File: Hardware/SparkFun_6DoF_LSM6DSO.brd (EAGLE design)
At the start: 25.4 x 25.4 mm, 61 parts, among them J1 QWIIC_RIGHT_ANGLE, J2 QWIIC_RIGHT_ANGLE, U2 LSM6DS0

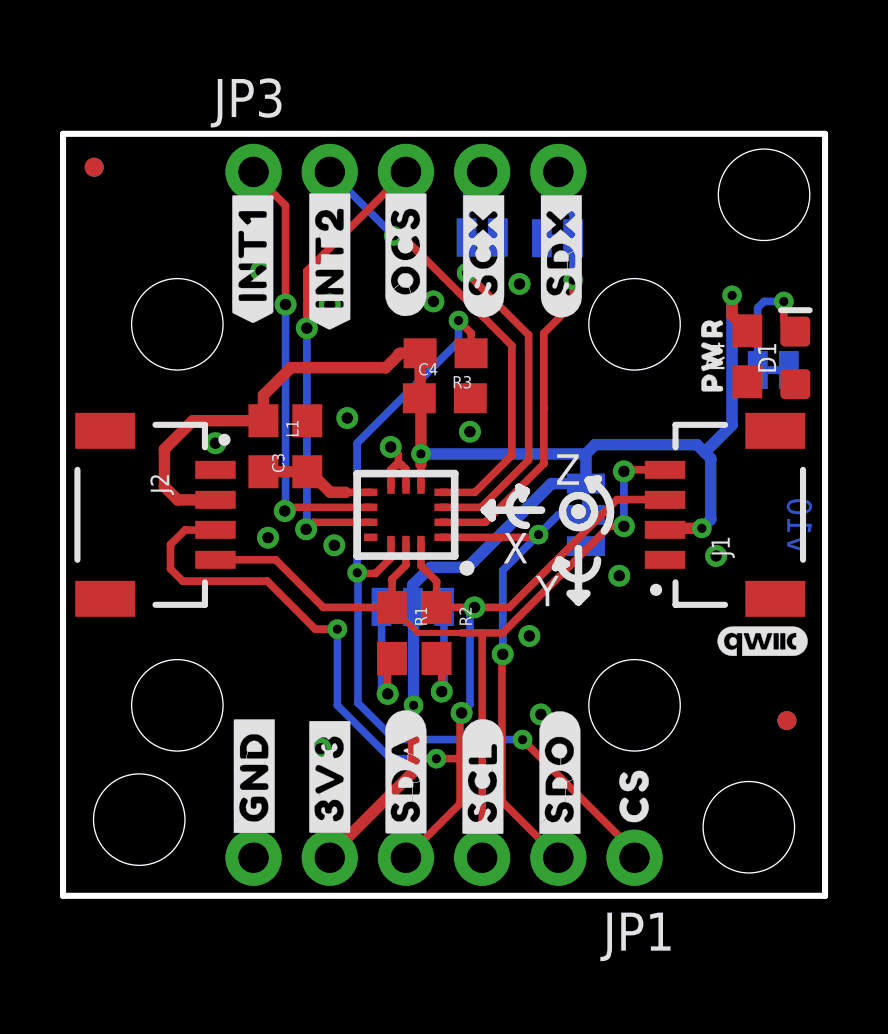
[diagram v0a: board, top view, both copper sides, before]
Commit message: Fixes input/output labels of respective silk, adds better text description to jumpers
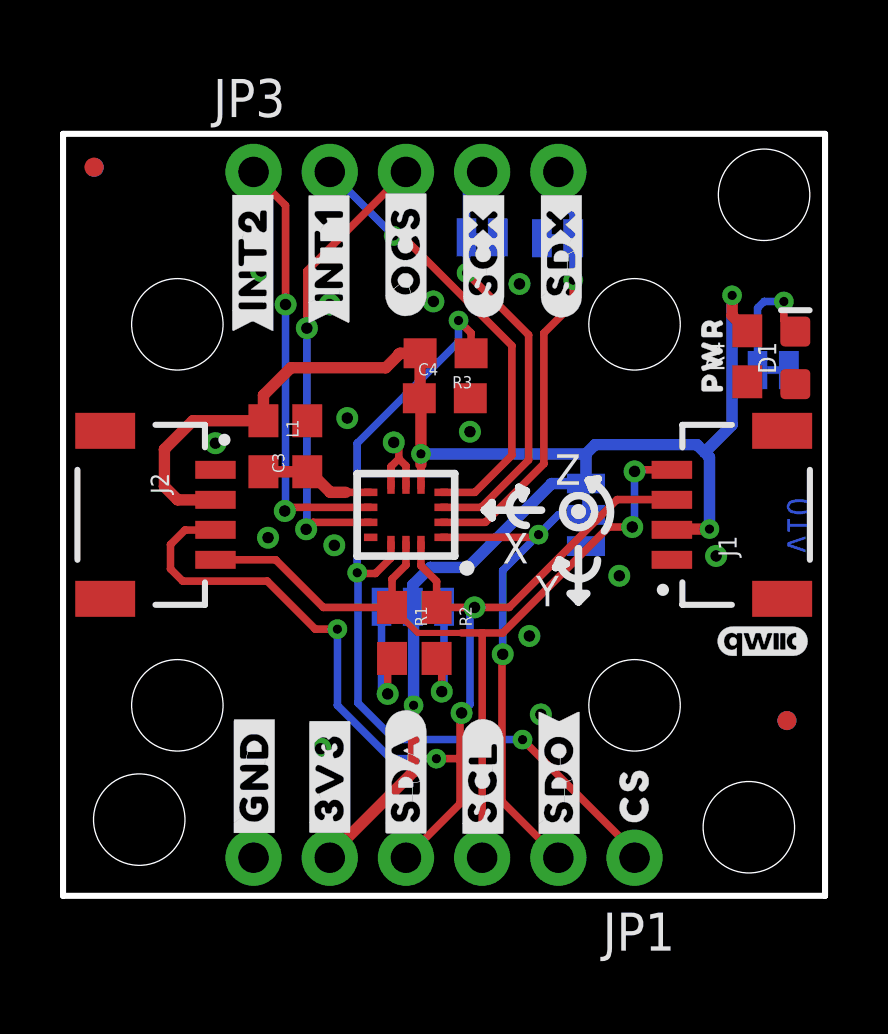
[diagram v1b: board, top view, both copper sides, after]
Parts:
- U$18: device bot:#INT1#7 -> bot:#SDO#7
- U$19: device bot:#INT2#7 -> bot:#INT1#9
- U$21: device bot:#SA0#7 -> bot:#INT2#9
- U$7: device top:#INT1#8 -> top:#INT1#9
- U$8: device top:#INT2#8 -> top:#INT2#9
- moved U$18 20.2 mm to (16.5, 3.94)
- moved U$21 20.1 mm to (6.32, 21.3)
- moved U$8 2.57 mm to (6.32, 21.3)
- moved U$7 2.54 mm to (8.86, 21.4)
- moved U$14 1.24 mm to (14.8, 13.3)
- moved U$13 1.14 mm to (14.7, 12.1)
- moved J1 0.23 mm to (20.3, 12.7)
- moved U$19 0.08 mm to (8.86, 21.4)
- renumbered JP2 to LED, U2 to U1

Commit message: Adds VDD and VDDIO voltage range to schematic
* Moves some traces and vias that were too close to the standoffs
* Adds SparkFun flame and name of product to topside
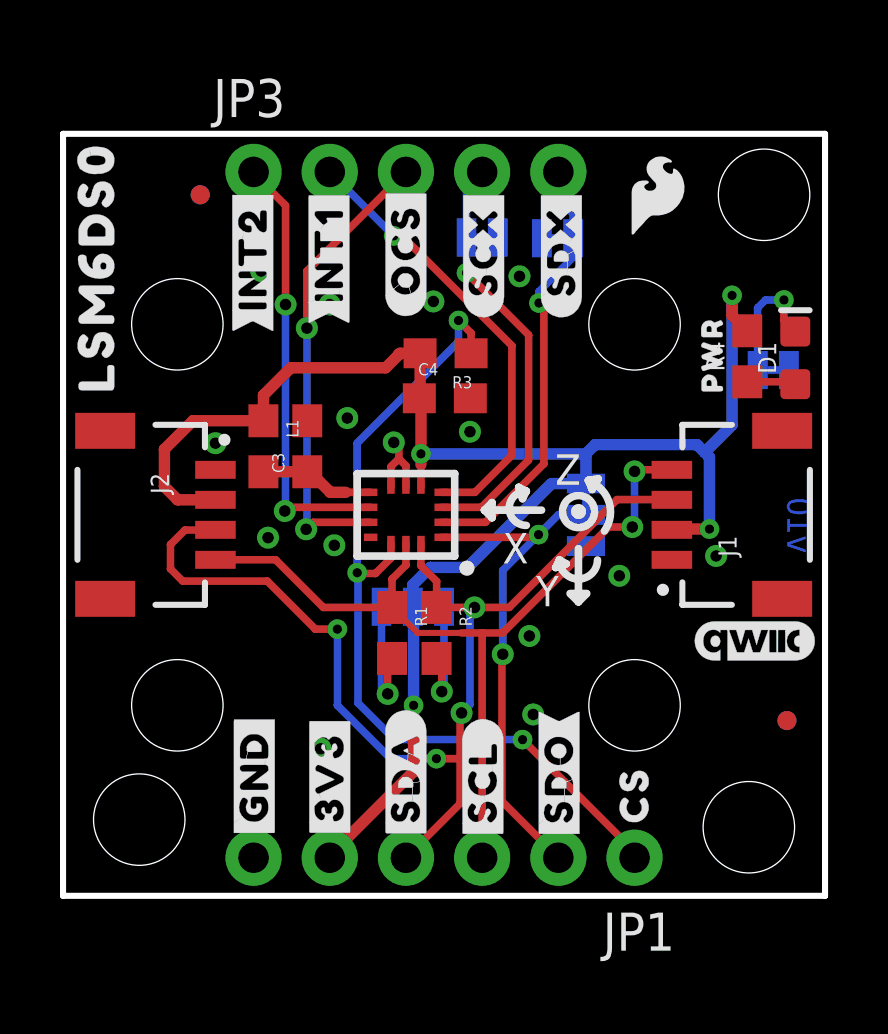
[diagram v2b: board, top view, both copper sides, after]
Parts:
- added U$29: (no value), SparkFun-Aesthetics:SFE_LOGO_FLAME_.1
- added U$30: (no value), top:LSM6DS011
- LOGO1: value QWIIC_LOGO_3MM -> QWIIC_LOGO_4MM; device SparkFun-Aesthetics:QWIIC_3MM -> SparkFun-Aesthetics:QWIIC_4MM
- moved FRAME1 17.8 mm to (-19.1, -11.4)
- moved FID1 3.66 mm to (4.57, 23.4)
- moved FD1 3.65 mm to (4.57, 23.4)
- moved LOGO1 0.25 mm to (23.1, 8.48)
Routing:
- net N$2: track 0.00 -> 1.63 mm
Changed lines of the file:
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@@
 <setting verticaltext="up"/>
 </settings>
-<grid distance="0.01" unitdist="inch" unit="inch" style="dots" multiple="1" display="yes" altdistance="0.001" altunitdist="inch" altunit="inch"/>
+<grid distance="0.05" unitdist="inch" unit="inch" style="dots" multiple="1" display="yes" altdistance="0.005" altunitdist="inch" altunit="inch"/>
 <layers>
 <layer number="1" name="Top" color="4" fill="1" visible="yes" active="yes"/>
@@
 <wire x1="5.3959125" y1="13.3937375" x2="6.1102875" y2="12.6793625" width="0.2032" layer="22"/>
 <wire x1="6.0706" y1="13.3937375" x2="5.356225" y2="12.6793625" width="0.2032" layer="22"/>
-<text x="-7.62" y="-31.75" size="1.778" layer="51" font="vector">Revised By: Elias Santistevan</text>
+<text x="-7.62" y="-13.97" size="1.778" layer="51" font="vector">Revised By: Elias Santistevan</text>
 <rectangle x1="15.7734" y1="22.86" x2="17.1958" y2="23.3934" layer="22"/>
 <rectangle x1="13.2334" y1="22.9108" x2="14.6304" y2="23.4188" layer="22"/>
@@
 </autorouter>
 <elements>
-<element name="FRAME1" library="SparkFun-Aesthetics" package="CREATIVE_COMMONS" value="FRAME-LETTER" x="-19.05" y="-29.21" smashed="yes">
-<attribute name="DESIGNER" value="Marshall Taylor" x="12.7" y="-29.21" size="1.778" layer="51" font="vector"/>
-<attribute name="REV" value="" x="-19.05" y="-29.21" size="1.778" layer="27" display="off"/>
+<element name="FRAME1" library="SparkFun-Aesthetics" package="CREATIVE_COMMONS" value="FRAME-LETTER" x="-19.05" y="-11.43" smashed="yes">
+<attribute name="DESIGNER" value="Marshall Taylor" x="12.7" y="-11.43" size="1.778" layer="51" font="vector"/>
+<attribute name="REV" value="" x="-19.05" y="-11.43" size="1.778" layer="27" display="off"/>
 </element>
 <element name="C3" library="SparkFun-Capacitors" package="0603" value="0.1uF" x="8.1407" y="14.986" smashed="yes" rot="R90">
@@
 <attribute name="VALUE" value="30Ω" x="5.5372" y="16.002" size="0.4064" layer="27" font="vector" rot="R270"/>
 </element>
-<element name="FID1" library="SparkFun-Aesthetics" package="FIDUCIAL-MICRO" value="FIDUCIALUFIDUCIAL" x="1.031875" y="24.28875" smashed="yes"/>
+<element name="FID1" library="SparkFun-Aesthetics" package="FIDUCIAL-MICRO" value="FIDUCIALUFIDUCIAL" x="4.572" y="23.368" smashed="yes"/>
 <element name="FID2" library="SparkFun-Aesthetics" package="FIDUCIAL-MICRO" value="FIDUCIALUFIDUCIAL" x="24.13" y="5.842" smashed="yes"/>
 <element name="R3" library="SparkFun-Resistors" package="0603" value="10k" x="12.7508" y="18.0848" smashed="yes" rot="R180">
@@
 <attribute name="VALUE" x="23.5966" y="11.049" size="0.6096" layer="27" font="vector" ratio="20" rot="R90"/>
 </element>
-<element name="FD1" library="SparkFun-Aesthetics" package="FIDUCIAL-MICRO" value="FIDUCIALUFIDUCIAL" x="1.0414" y="24.2824" smashed="yes" rot="MR0"/>
+<element name="FD1" library="SparkFun-Aesthetics" package="FIDUCIAL-MICRO" value="FIDUCIALUFIDUCIAL" x="4.572" y="23.368" smashed="yes" rot="MR0"/>
 <element name="FD2" library="SparkFun-Aesthetics" package="FIDUCIAL-MICRO" value="FIDUCIALUFIDUCIAL" x="24.13" y="5.842" smashed="yes" rot="MR0"/>
-<element name="LOGO1" library="SparkFun-Aesthetics" package="QWIIC_3MM" value="QWIIC_LOGO_3MM" x="23.3172" y="8.4836" smashed="yes"/>
+<element name="LOGO1" library="SparkFun-Aesthetics" package="QWIIC_4MM" value="QWIIC_LOGO_4MM" x="23.0632" y="8.4836" smashed="yes"/>
 <element name="U$1" library="top" package="#3V3#1" value="" x="8.89" y="3.9624" smashed="yes" rot="R90"/>
 <element name="U$2" library="top" package="#GND#0" value="" x="6.3754" y="3.9878" smashed="yes" rot="R90"/>
@@
 <element name="U$21" library="bot" package="#INT2#9" value="" x="6.3246" y="21.2598" smashed="yes" rot="MR270"/>
 <element name="U$26" library="bot" package="#SDI#4" value="" x="11.43" y="3.6068" smashed="yes" rot="MR270"/>
+<element name="U$29" library="SparkFun-Aesthetics" package="SFE_LOGO_FLAME_.1" value="" x="19.812" y="23.368" smashed="yes"/>
+<element name="U$30" library="top" package="LSM6DS011" value="" x="1.1176" y="20.9804" smashed="yes" rot="R90"/>
 </elements>
 <signals>
@@
 <contactref element="J1" pad="1"/>
 <via x="9.4742" y="15.9258" extent="1-16" drill="0.381"/>
-<via x="15.2146" y="20.3962" extent="1-16" drill="0.381"/>
+<via x="15.2146" y="20.6502" extent="1-16" drill="0.381"/>
 <via x="18.542" y="10.668" extent="1-16" drill="0.381"/>
 <via x="8.5852" y="4.9022" extent="1-16" drill="0.381"/>
@@
 <via x="5.08" y="15.0876" extent="1-16" drill="0.381"/>
 <via x="13.5636" y="15.4686" extent="1-16" drill="0.381"/>
-<via x="15.9258" y="6.0452" extent="1-16" drill="0.381"/>
+<via x="15.6718" y="6.0452" extent="1-16" drill="0.381"/>
 <via x="15.5448" y="8.6614" extent="1-16" drill="0.381"/>
 <via x="12.3444" y="19.812" extent="1-16" drill="0.381"/>
@@
 <contactref element="SDX" pad="2"/>
 <wire x1="14.0756" y1="12.45" x2="16.0274" y2="14.4018" width="0.254" layer="1"/>
-<wire x1="17.0053" y1="20.5232" x2="17.0053" y2="21.9202" width="0.254" layer="16"/>
-<wire x1="17.0053" y1="20.5232" x2="17.0053" y2="19.7358" width="0.254" layer="1"/>
-<wire x1="17.0053" y1="19.7358" x2="16.0274" y2="18.7579" width="0.254" layer="1"/>
-<wire x1="16.0274" y1="18.7579" x2="16.0274" y2="14.4018" width="0.254" layer="1"/>
+<wire x1="17.0053" y1="21.2852" x2="17.0053" y2="21.9202" width="0.254" layer="16"/>
+<wire x1="17.0053" y1="21.2852" x2="15.8623" y2="20.1422" width="0.254" layer="16"/>
+<wire x1="15.8623" y1="20.1422" x2="15.8623" y2="19.7612" width="0.254" layer="16"/>
+<wire x1="15.8623" y1="19.7612" x2="16.0274" y2="19.5961" width="0.254" layer="1"/>
+<wire x1="16.0274" y1="19.5961" x2="16.0274" y2="14.4018" width="0.254" layer="1"/>
 <wire x1="17.0053" y1="21.9202" x2="17.0053" y2="22.733" width="0.254" layer="16"/>
 <wire x1="17.0053" y1="22.733" x2="16.51" y2="23.2283" width="0.254" layer="16"/>
 <wire x1="16.51" y1="23.2283" x2="16.51" y2="24.13" width="0.254" layer="16"/>
-<via x="17.0053" y="20.5232" extent="1-16" drill="0.3048"/>
+<via x="15.8623" y="19.7612" extent="1-16" drill="0.3048"/>
 <contactref element="U1" pad="2"/>
 <wire x1="12.605" y1="12.45" x2="14.0756" y2="12.45" width="0.254" layer="1"/>
@@
 <wire x1="17.43075" y1="14.732" x2="17.73555" y2="15.0368" width="0.381" layer="16"/>
 <wire x1="17.73555" y1="15.0368" x2="21.1328" y2="15.0368" width="0.381" layer="16"/>
-<wire x1="11.93" y1="14.3764" x2="11.938" y2="14.3764" width="0.254" layer="1"/>
 <wire x1="11.93" y1="14.732" x2="11.93" y2="14.3764" width="0.381" layer="1"/>
 <contactref element="R4" pad="2"/>
@@
 <contactref element="R4" pad="1"/>
 <contactref element="D1" pad="A"/>
-<wire x1="22.8092" y1="17.1332" x2="24.4094" y2="17.0554" width="0" layer="19" extent="1-1"/>
+<wire x1="22.8092" y1="17.1332" x2="24.3316" y2="17.1332" width="0.254" layer="1"/>
+<wire x1="24.3316" y1="17.1332" x2="24.4094" y2="17.0554" width="0.254" layer="1"/>
 </signal>
 <signal name="N$3">
@@
 <contactref element="LED" pad="2"/>
 <wire x1="24.4094" y1="18.8094" x2="24.0284" y2="19.1904" width="0.254" layer="1"/>
-<wire x1="24.0284" y1="19.1904" x2="24.0284" y2="19.812" width="0.254" layer="1"/>
-<via x="24.0284" y="19.812" extent="1-16" drill="0.3048"/>
-<wire x1="24.0284" y1="19.812" x2="23.368" y2="19.812" width="0.254" layer="16"/>
-<wire x1="23.368" y1="19.812" x2="23.1521" y2="19.5961" width="0.254" layer="16"/>
+<wire x1="24.0284" y1="19.1904" x2="24.0284" y2="19.8628" width="0.254" layer="1"/>
+<via x="24.0284" y="19.8628" extent="1-16" drill="0.3048"/>
+<wire x1="24.0284" y1="19.8628" x2="23.4188" y2="19.8628" width="0.254" layer="16"/>
+<wire x1="23.4188" y1="19.8628" x2="23.1521" y2="19.5961" width="0.254" layer="16"/>
 <wire x1="23.1521" y1="19.5961" x2="23.1521" y2="17.526" width="0.254" layer="16"/>
 </signal>

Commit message: Updates LSM6D0 with axes, fixes measures, removes references to "slave/master" terminology
* Removes inner standoffs
* Centers IC
* Adds 100k pullup to SDO/SA0 net
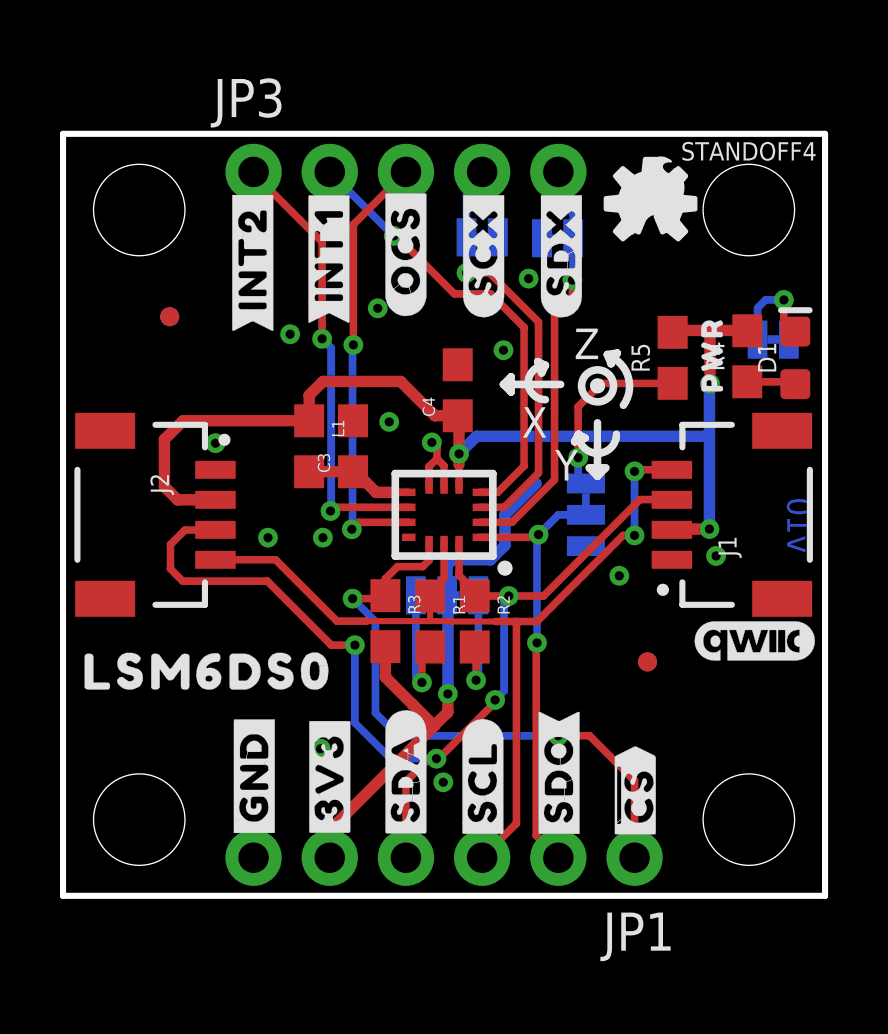
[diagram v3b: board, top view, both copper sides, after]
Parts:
- removed STANDOFF5, STANDOFF6, STANDOFF7: STAND-OFFTIGHT, SparkFun-Hardware:STAND-OFF-TIGHT
- added R5: 100k, SparkFun-Resistors:0603
- added U$31: (no value), top:6DOF12
- U$27: device top:CS7 -> bot:##CS##8
- U$3: device bot:CS7 -> top:##CS##7
- moved LOGO2 17.0 mm to (19.6, 23.1), flipped to the top
- moved STANDOFF3 16.9 mm to (22.9, 2.54)
- moved STANDOFF4 16.9 mm to (22.9, 22.9)
- moved U$30 14.0 mm to (4.85, 7.47), turned to 0 degrees
- moved R3 9.15 mm to (10.7, 9.16), turned to 270 degrees
- moved U$12 6.26 mm to (7.59, 11.9)
- moved LOGO3 6.22 mm to (4.12, 12.8), turned to 270 degrees
- moved FD2 5.04 mm to (19.5, 7.80)
- moved FID2 5.04 mm to (19.5, 7.80)
- moved FD1 4.19 mm to (3.56, 19.3)
- moved FID1 4.19 mm to (3.56, 19.3)
- moved STANDOFF2 4.02 mm to (2.54, 2.54)
- moved STANDOFF1 4.02 mm to (2.54, 22.9)
- moved L1 1.52 mm to (8.20, 15.0)
- moved C3 1.52 mm to (9.66, 15.0)
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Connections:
- net CS renamed !CS!
- new net N$1: ADDR.3, R5.1
- net 3.3V: now also R5.2; no longer ADDR.3
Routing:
- net !CS!: track 28.8 -> 20.3 mm, vias 3 -> 2
- net N$1: track 0.00 -> 6.14 mm, vias 0 -> 1
- net SDO/SA0: track 17.2 -> 15.0 mm
- net SCL: track 29.4 -> 31.0 mm
- net SDA: track 37.3 -> 36.0 mm
- net N$3: track 4.27 -> 3.25 mm
- net 3.3V: track 57.0 -> 56.1 mm
- net SDX: track 14.7 -> 13.8 mm
- net OCS: track 15.5 -> 14.7 mm
- net GND: vias 15 -> 13
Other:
- board text removed: "Units in Inches"

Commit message: Fixes silk overlap
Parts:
- moved LOGO2 0.27 mm to (19.7, 23.3), flipped to the bottom
- moved U$29 0.18 mm to (19.7, 23.2)
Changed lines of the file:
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@@
 <setting verticaltext="up"/>
 </settings>
-<grid distance="0.01" unitdist="inch" unit="inch" style="dots" multiple="1" display="yes" altdistance="0.001" altunitdist="inch" altunit="inch"/>
+<grid distance="0.05" unitdist="inch" unit="inch" style="dots" multiple="1" display="yes" altdistance="0.005" altunitdist="inch" altunit="inch"/>
 <layers>
 <layer number="1" name="Top" color="4" fill="1" visible="yes" active="yes"/>
@@
 <layer number="45" name="Holes" color="7" fill="1" visible="yes" active="yes"/>
 <layer number="46" name="Milling" color="3" fill="1" visible="no" active="yes"/>
-<layer number="47" name="Measures" color="7" fill="1" visible="yes" active="yes"/>
+<layer number="47" name="Measures" color="7" fill="1" visible="no" active="yes"/>
 <layer number="48" name="Document" color="7" fill="1" visible="no" active="yes"/>
 <layer number="49" name="Reference" color="13" fill="1" visible="yes" active="yes"/>
@@
 <attribute name="VALUE" x="14.3002" y="15.8369" size="0.4064" layer="27" font="vector" rot="R90"/>
 </element>
-<element name="LOGO2" library="SparkFun-Aesthetics" package="OSHW-LOGO-S" value="OSHW-LOGOS" x="19.5834" y="23.06955" smashed="yes"/>
+<element name="LOGO2" library="SparkFun-Aesthetics" package="OSHW-LOGO-S" value="OSHW-LOGOS" x="19.6596" y="23.32355" smashed="yes" rot="MR0"/>
 <element name="STANDOFF1" library="SparkFun-Hardware" package="STAND-OFF-TIGHT" value="STAND-OFFTIGHT" x="2.54" y="22.86" smashed="yes"/>
 <element name="STANDOFF2" library="SparkFun-Hardware" package="STAND-OFF-TIGHT" value="STAND-OFFTIGHT" x="2.54" y="2.54" smashed="yes"/>
@@
 <element name="U$21" library="bot" package="#INT2#9" value="" x="6.3246" y="21.2598" smashed="yes" rot="MR270"/>
 <element name="U$26" library="bot" package="#SDI#4" value="" x="11.43" y="3.6068" smashed="yes" rot="MR270"/>
-<element name="U$29" library="SparkFun-Aesthetics" package="SFE_LOGO_FLAME_.1" value="" x="19.812" y="23.368" smashed="yes"/>
 <element name="U$30" library="top" package="LSM6DS011" value="" x="4.8514" y="7.4676" smashed="yes"/>
 <element name="STANDOFF4" library="SparkFun-Hardware" package="STAND-OFF-TIGHT" value="STAND-OFFTIGHT" x="22.86" y="22.86" smashed="yes">
@@
 <attribute name="VALUE" x="21.082" y="17.9324" size="0.6096" layer="27" font="vector" ratio="20" rot="R90" align="top-center"/>
 </element>
+<element name="U$29" library="SparkFun-Aesthetics" package="SFE_LOGO_FLAME_.1" value="" x="19.685" y="23.241" smashed="yes"/>
 </elements>
 <signals>
